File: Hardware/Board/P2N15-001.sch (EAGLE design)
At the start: 30 parts, among them IC1 TLC5941NT, IC2 LTC485N, IC3 74LS07N, IC4 LTC485N

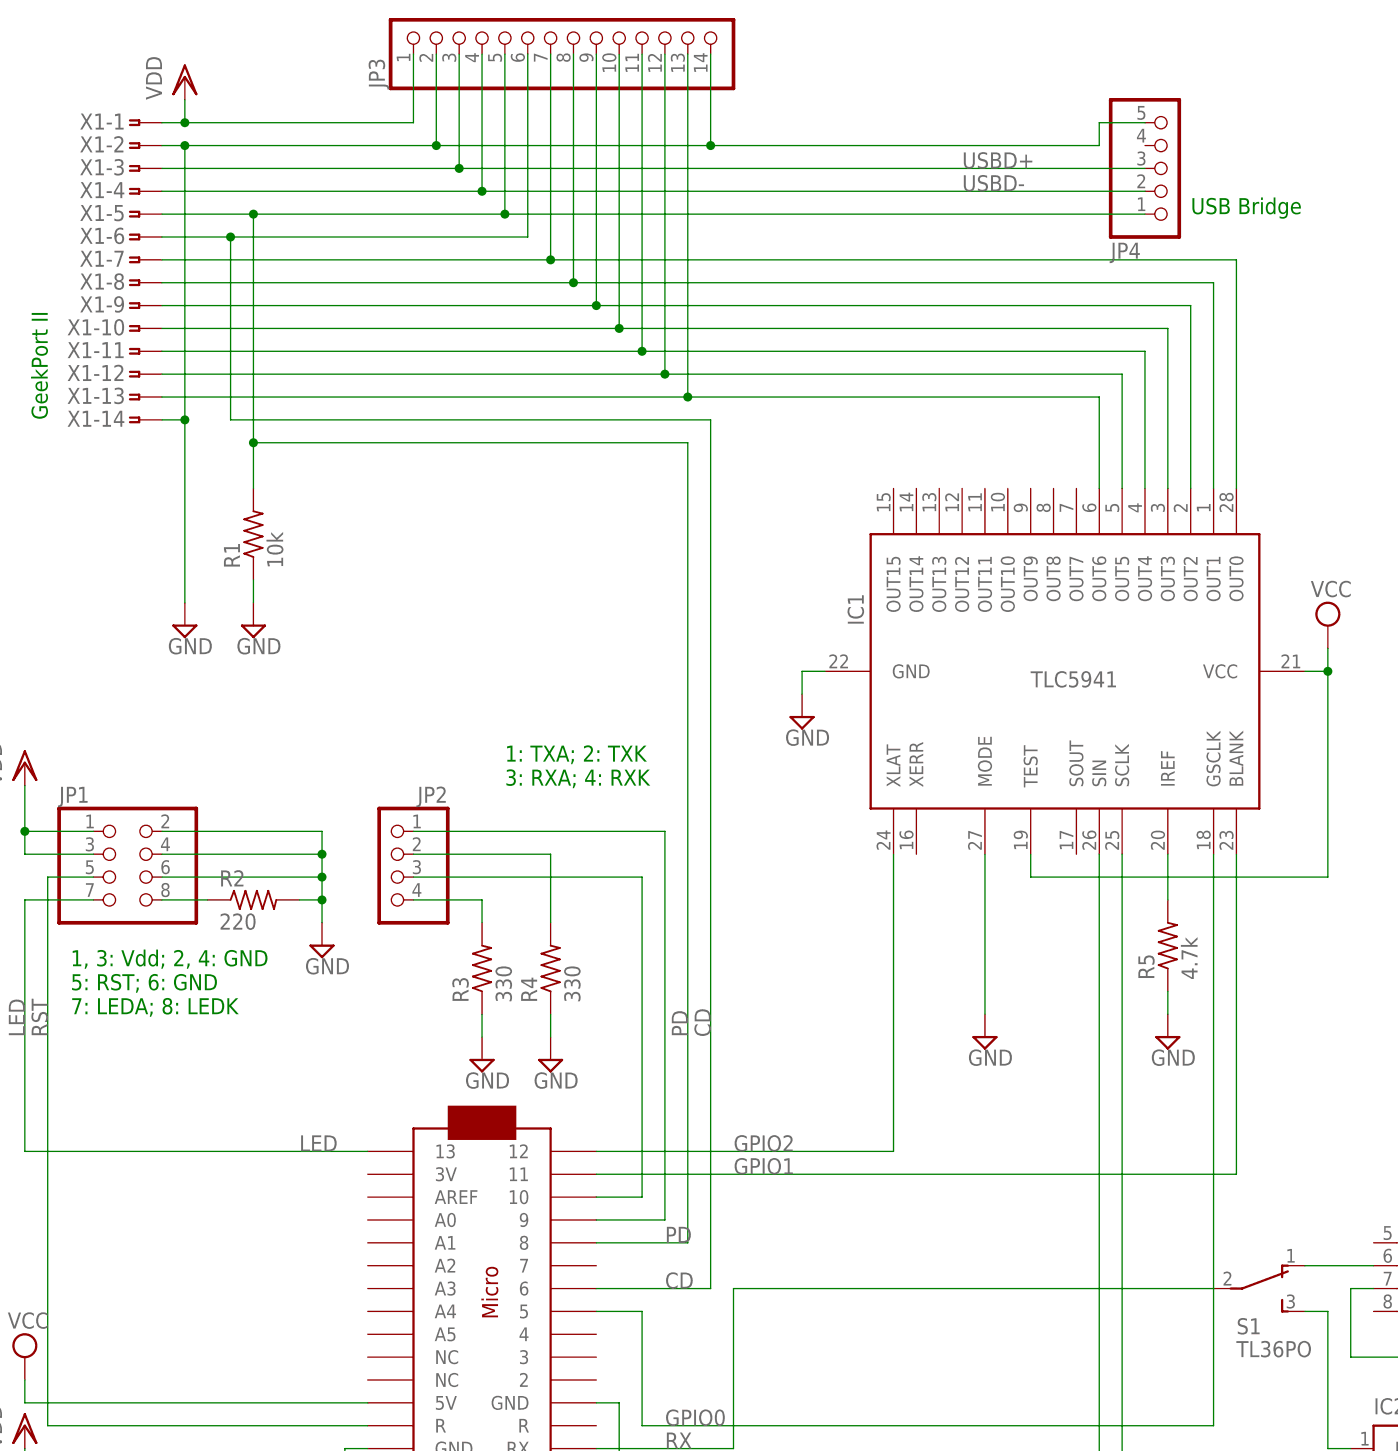
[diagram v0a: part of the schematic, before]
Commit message: Attached LED pattern to GPIO pins.
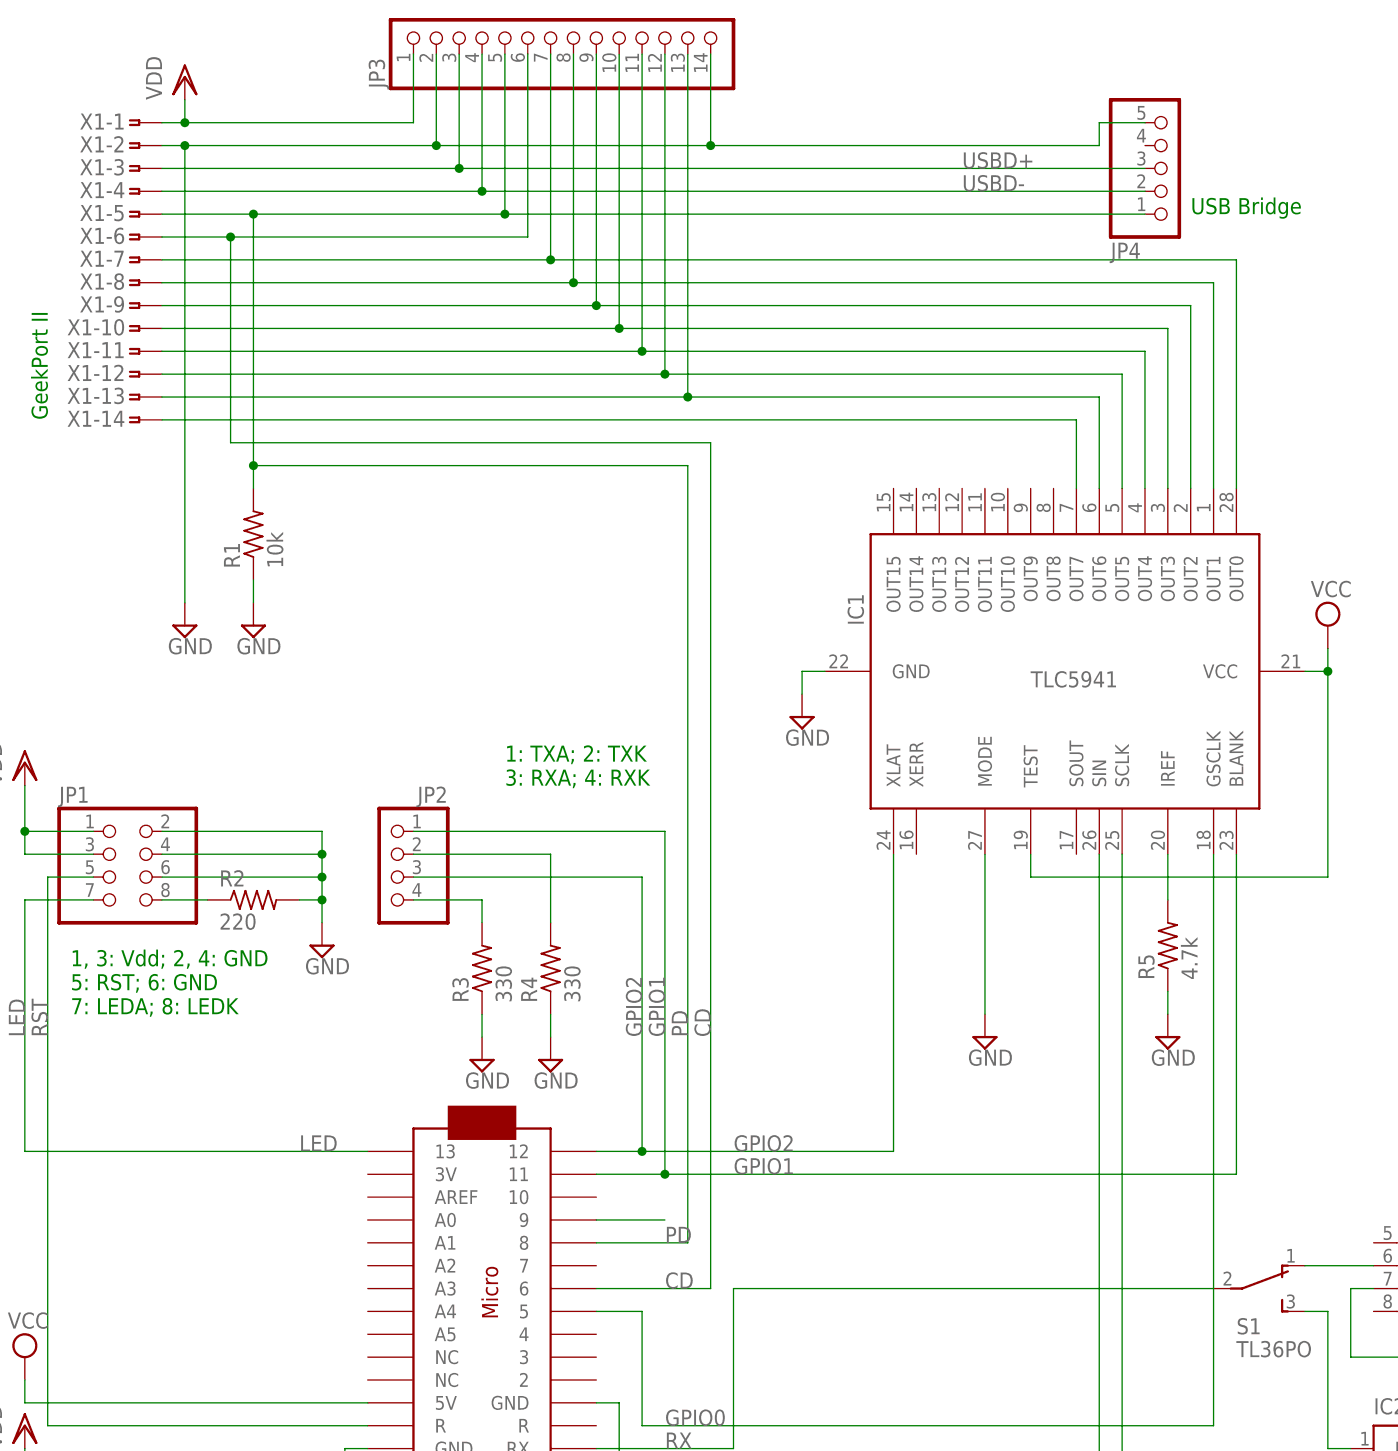
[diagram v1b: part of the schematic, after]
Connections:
- removed net N$5: JP2.3, MC1.10
- new net N$8: IC1.OUT7, X1-14.1
- net GND: no longer X1-14.1
- net GPIO1: now also JP2.1
- net GPIO2: now also JP2.3
- net N$3: no longer JP2.1
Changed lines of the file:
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@@
 <pinref part="SUPPLY2" gate="GND" pin="GND"/>
 <wire x1="22.86" y1="182.88" x2="25.4" y2="182.88" width="0.1524" layer="91"/>
-<wire x1="25.4" y1="182.88" x2="25.4" y2="152.4" width="0.1524" layer="91"/>
-<pinref part="X1" gate="-14" pin="1"/>
-<wire x1="25.4" y1="152.4" x2="25.4" y2="132.08" width="0.1524" layer="91"/>
-<wire x1="22.86" y1="152.4" x2="25.4" y2="152.4" width="0.1524" layer="91"/>
-<junction x="25.4" y="152.4"/>
+<wire x1="25.4" y1="182.88" x2="25.4" y2="132.08" width="0.1524" layer="91"/>
 <wire x1="25.4" y1="182.88" x2="53.34" y2="182.88" width="0.1524" layer="91"/>
 <wire x1="53.34" y1="182.88" x2="83.82" y2="182.88" width="0.1524" layer="91"/>
@@
 <segment>
 <pinref part="MC1" gate="G$1" pin="11"/>
-<wire x1="71.12" y1="68.58" x2="142.24" y2="68.58" width="0.1524" layer="91"/>
+<wire x1="71.12" y1="68.58" x2="78.74" y2="68.58" width="0.1524" layer="91"/>
 <label x="86.36" y="68.58" size="1.778" layer="95"/>
 <pinref part="IC1" gate="G$1" pin="BLANK"/>
+<wire x1="78.74" y1="68.58" x2="142.24" y2="68.58" width="0.1524" layer="91"/>
 <wire x1="142.24" y1="68.58" x2="142.24" y2="104.14" width="0.1524" layer="91"/>
+<pinref part="JP2" gate="A" pin="1"/>
+<wire x1="50.8" y1="106.68" x2="78.74" y2="106.68" width="0.1524" layer="91"/>
+<wire x1="78.74" y1="106.68" x2="78.74" y2="68.58" width="0.1524" layer="91"/>
+<junction x="78.74" y="68.58"/>
+<label x="78.74" y="83.82" size="1.778" layer="95" rot="R90"/>
 </segment>
 </net>
@@
 <wire x1="33.02" y1="175.26" x2="60.96" y2="175.26" width="0.1524" layer="91"/>
 <wire x1="60.96" y1="175.26" x2="132.08" y2="175.26" width="0.1524" layer="91"/>
-<wire x1="33.02" y1="175.26" x2="33.02" y2="149.86" width="0.1524" layer="91"/>
+<wire x1="33.02" y1="175.26" x2="33.02" y2="147.32" width="0.1524" layer="91"/>
 <pinref part="R1" gate="G$1" pin="2"/>
 <junction x="33.02" y="175.26"/>
-<wire x1="33.02" y1="149.86" x2="33.02" y2="144.78" width="0.1524" layer="91"/>
-<wire x1="33.02" y1="149.86" x2="81.28" y2="149.86" width="0.1524" layer="91"/>
-<junction x="33.02" y="149.86"/>
-<wire x1="81.28" y1="149.86" x2="81.28" y2="60.96" width="0.1524" layer="91"/>
+<wire x1="33.02" y1="147.32" x2="33.02" y2="144.78" width="0.1524" layer="91"/>
+<wire x1="33.02" y1="147.32" x2="81.28" y2="147.32" width="0.1524" layer="91"/>
+<junction x="33.02" y="147.32"/>
+<wire x1="81.28" y1="147.32" x2="81.28" y2="60.96" width="0.1524" layer="91"/>
 <pinref part="MC1" gate="G$1" pin="8"/>
 <wire x1="81.28" y1="60.96" x2="71.12" y2="60.96" width="0.1524" layer="91"/>
@@
 <pinref part="X1" gate="-6" pin="1"/>
 <wire x1="22.86" y1="172.72" x2="30.48" y2="172.72" width="0.1524" layer="91"/>
-<wire x1="30.48" y1="172.72" x2="30.48" y2="152.4" width="0.1524" layer="91"/>
-<wire x1="30.48" y1="152.4" x2="83.82" y2="152.4" width="0.1524" layer="91"/>
-<wire x1="83.82" y1="152.4" x2="83.82" y2="55.88" width="0.1524" layer="91"/>
+<wire x1="30.48" y1="172.72" x2="30.48" y2="149.86" width="0.1524" layer="91"/>
+<wire x1="30.48" y1="149.86" x2="83.82" y2="149.86" width="0.1524" layer="91"/>
+<wire x1="83.82" y1="149.86" x2="83.82" y2="55.88" width="0.1524" layer="91"/>
 <pinref part="MC1" gate="G$1" pin="6"/>
 <wire x1="83.82" y1="55.88" x2="71.12" y2="55.88" width="0.1524" layer="91"/>
@@
 <segment>
 <pinref part="MC1" gate="G$1" pin="12"/>
-<wire x1="71.12" y1="71.12" x2="104.14" y2="71.12" width="0.1524" layer="91"/>
+<wire x1="71.12" y1="71.12" x2="76.2" y2="71.12" width="0.1524" layer="91"/>
 <label x="86.36" y="71.12" size="1.778" layer="95"/>
 <pinref part="IC1" gate="G$1" pin="XLAT"/>
+<wire x1="76.2" y1="71.12" x2="104.14" y2="71.12" width="0.1524" layer="91"/>
 <wire x1="104.14" y1="71.12" x2="104.14" y2="104.14" width="0.1524" layer="91"/>
+<pinref part="JP2" gate="A" pin="3"/>
+<wire x1="50.8" y1="101.6" x2="76.2" y2="101.6" width="0.1524" layer="91"/>
+<wire x1="76.2" y1="101.6" x2="76.2" y2="71.12" width="0.1524" layer="91"/>
+<junction x="76.2" y="71.12"/>
+<label x="76.2" y="83.82" size="1.778" layer="95" rot="R90"/>
 </segment>
 </net>
@@
 <pinref part="MC1" gate="G$1" pin="9"/>
 <wire x1="71.12" y1="63.5" x2="78.74" y2="63.5" width="0.1524" layer="91"/>
-<pinref part="JP2" gate="A" pin="1"/>
-<wire x1="50.8" y1="106.68" x2="78.74" y2="106.68" width="0.1524" layer="91"/>
-<wire x1="78.74" y1="106.68" x2="78.74" y2="63.5" width="0.1524" layer="91"/>
-</segment>
-</net>
-<net name="N$5" class="0">
-<segment>
-<pinref part="JP2" gate="A" pin="3"/>
-<wire x1="50.8" y1="101.6" x2="76.2" y2="101.6" width="0.1524" layer="91"/>
-<wire x1="76.2" y1="101.6" x2="76.2" y2="66.04" width="0.1524" layer="91"/>
-<pinref part="MC1" gate="G$1" pin="10"/>
-<wire x1="76.2" y1="66.04" x2="71.12" y2="66.04" width="0.1524" layer="91"/>
 </segment>
 </net>
@@
 </segment>
 </net>
+<net name="N$8" class="0">
+<segment>
+<pinref part="X1" gate="-14" pin="1"/>
+<pinref part="IC1" gate="G$1" pin="OUT7"/>
+<wire x1="22.86" y1="152.4" x2="124.46" y2="152.4" width="0.1524" layer="91"/>
+<wire x1="124.46" y1="152.4" x2="124.46" y2="144.78" width="0.1524" layer="91"/>
+</segment>
+</net>

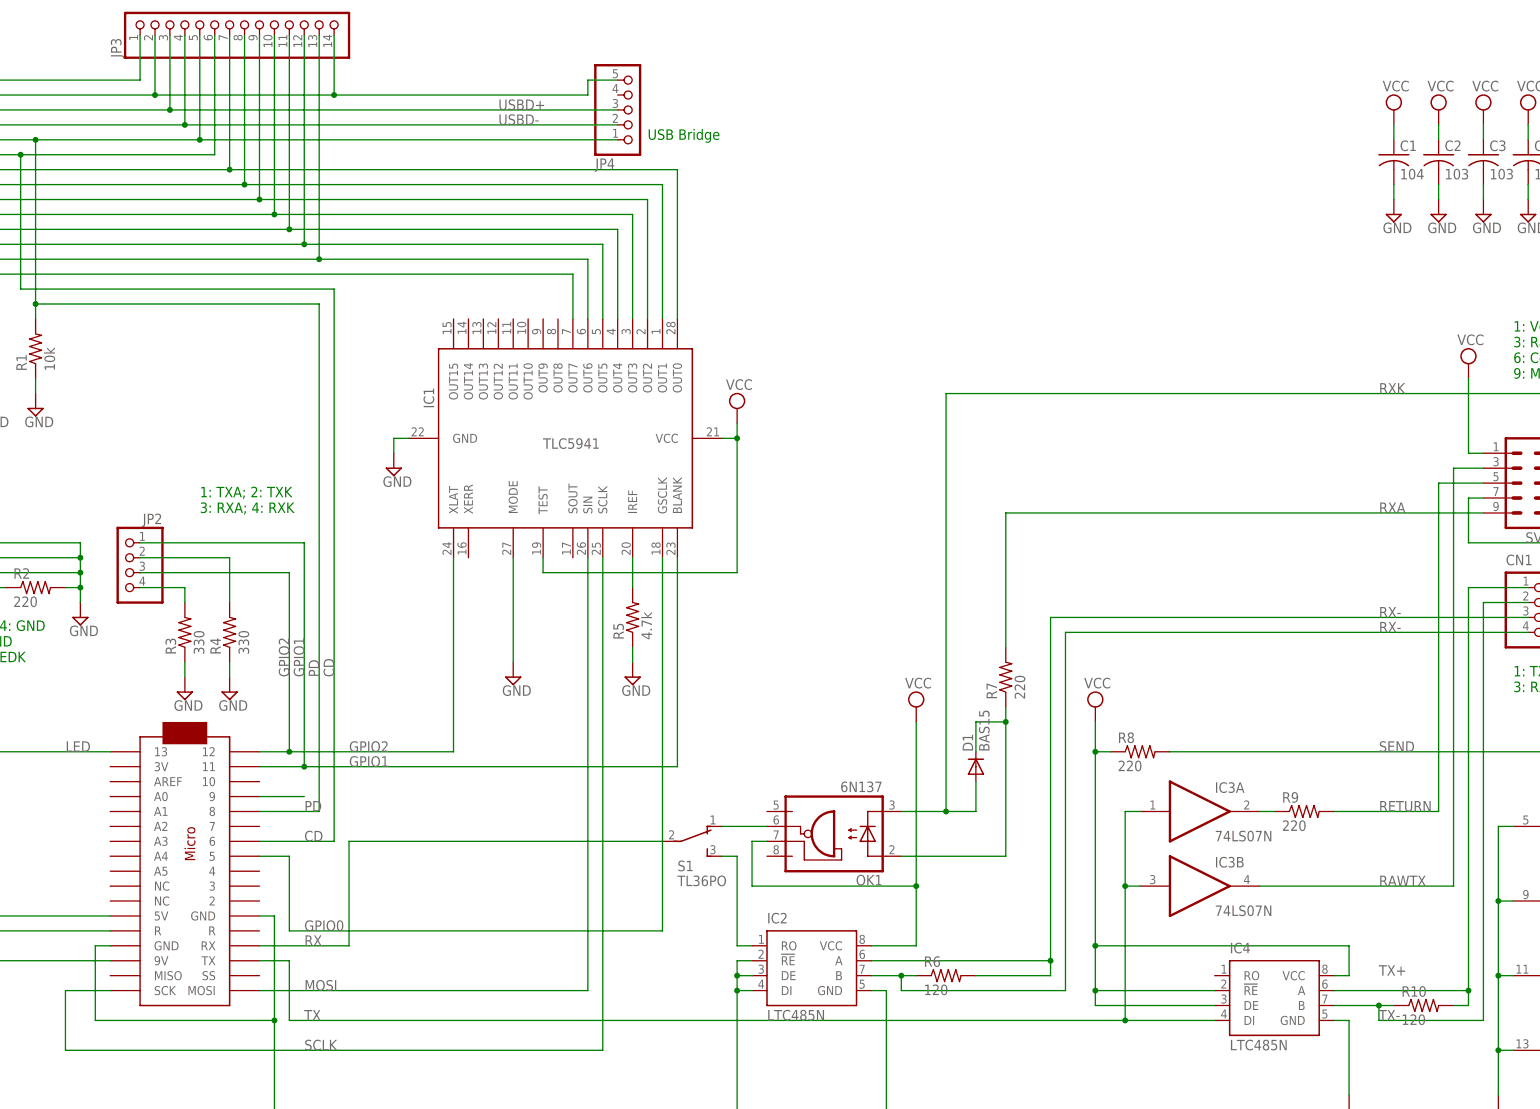
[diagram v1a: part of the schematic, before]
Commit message: Added LED monitors to P2N15.
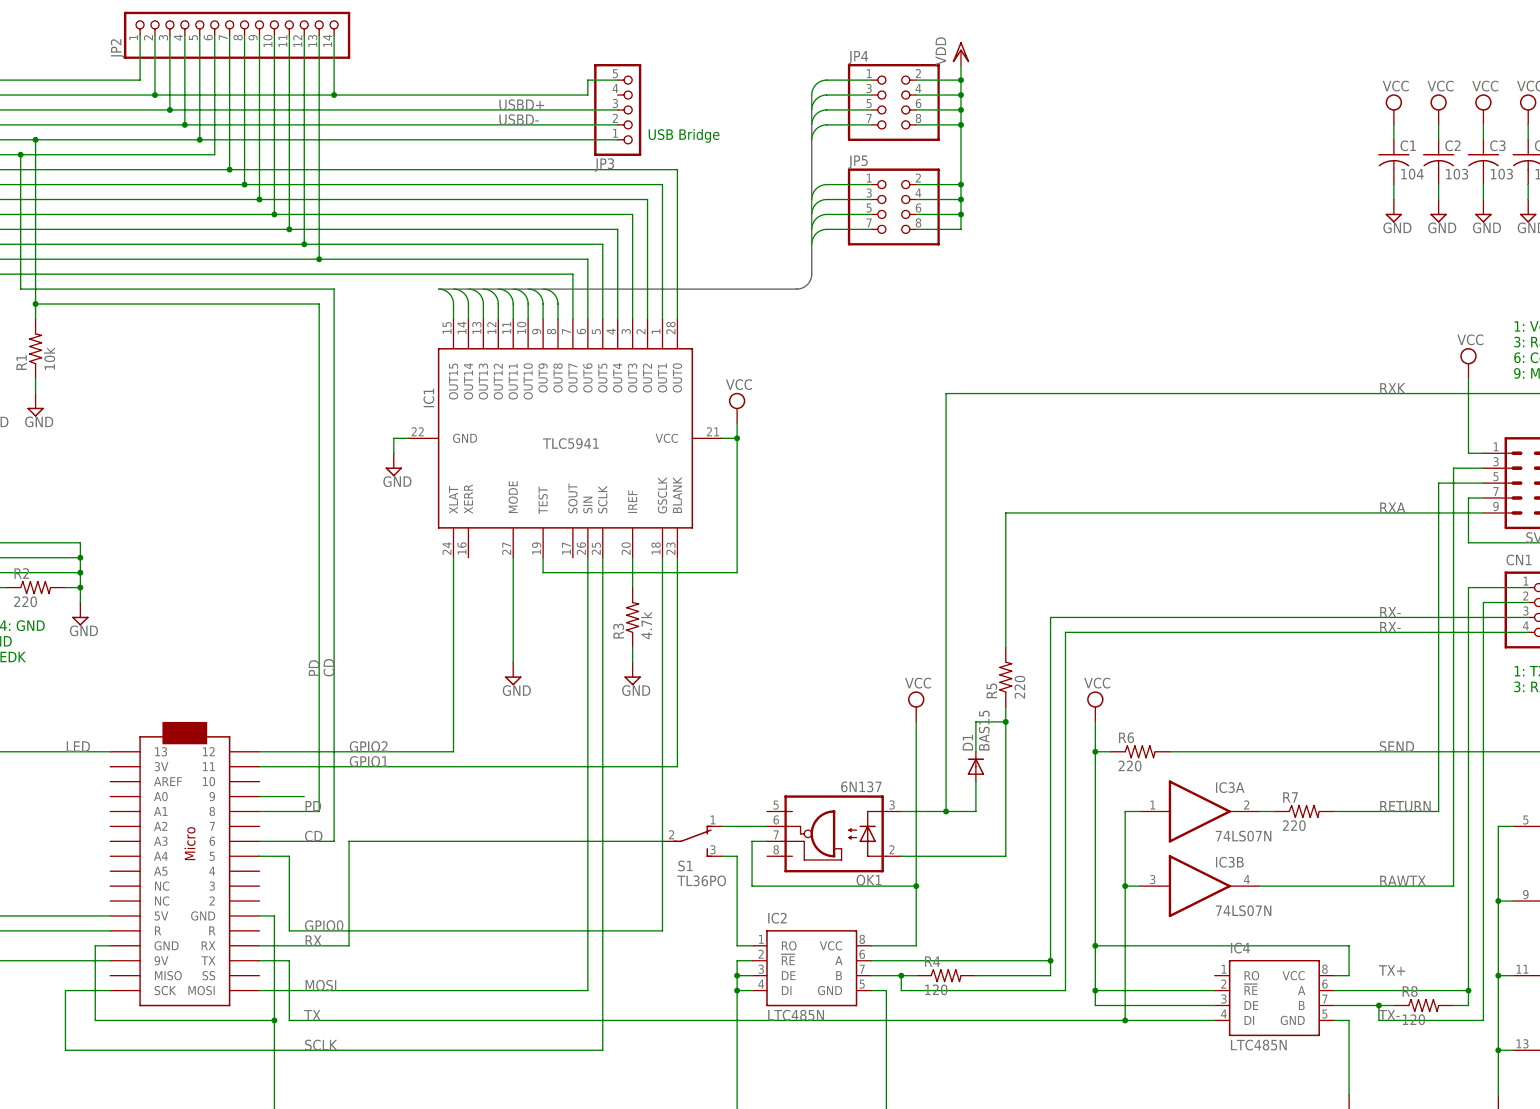
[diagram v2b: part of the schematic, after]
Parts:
- removed R10: 120, resistor:R-US_0204/5
- removed R9: 220, resistor:R-US_0204/5
- added JP5: (no value), pinhead:PINHD-2X4
- JP2: device pinhead:PINHD-1X4 -> pinhead:PINHD-1X14
- JP3: device pinhead:PINHD-1X14 -> pinhead:PINHD-1X5/90
- JP4: device pinhead:PINHD-1X5/90 -> pinhead:PINHD-2X4
- R3: value 330 -> 4.7k
- R4: value 330 -> 120
- R5: value 4.7k -> 220
- R6: value 120 -> 220
- R8: value 220 -> 120
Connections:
- removed net N$6: JP2.2, R4.2
- removed net N$7: JP2.4, R3.2
- new net LED0: IC1.OUT8, JP4.1
- new net LED1: IC1.OUT9, JP4.3
- new net LED2: IC1.OUT10, JP4.5
- new net LED3: IC1.OUT11, JP4.7
- new net LED4: IC1.OUT12, JP5.1
- new net LED5: IC1.OUT13, JP5.3
- new net LED6: IC1.OUT14, JP5.5
- new net LED7: IC1.OUT15, JP5.7
- net ANLG0: now also JP2.8; no longer JP3.8
- net ANLG1: now also JP2.9; no longer JP3.9
- net ANLG2: now also JP2.10; no longer JP3.10
- net ANLG3: now also JP2.11; no longer JP3.11
- net CD: now also JP2.6; no longer JP3.6
- net GND: now also JP2.14, JP2.2, JP3.5; no longer JP3.14, JP3.2, JP4.5, R4.1, R5.1
- net GPIO1: no longer JP2.1
- net GPIO2: no longer JP2.3
- net N$1: now also JP2.7; no longer JP3.7
- net N$15: now also R5.1; no longer R7.1
- net N$2: now also R7.1; no longer R9.1
- net N$28: now also JP2.12; no longer JP3.12
- net N$29: now also JP2.13; no longer JP3.13
- net N$4: now also R3.2; no longer R5.2
- net PD: now also JP2.5, JP3.1; no longer JP3.5, JP4.1
- net RETURN: now also R7.2; no longer R9.2
- net RX+: now also R4.2; no longer R6.2
- net RX-: now also R4.1; no longer R6.1
- net RXA: now also R5.2; no longer R7.2
- net SEND: now also R6.2; no longer R8.2
- net TX+: now also R8.2; no longer R10.2
- net TX-: now also R8.1; no longer R10.1
- net USBD+: now also JP2.3; no longer JP4.3
- net USBD-: now also JP2.4, JP3.2; no longer JP3.4, JP4.2
- net VCC: now also R6.1; no longer R8.1
- net VDD: now also JP2.1, JP4.2, JP4.4, JP4.6, JP4.8, JP5.2, JP5.4, JP5.6, JP5.8; no longer JP3.1
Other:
- note removed: "1: TXA; 2: TXK 3: RXA; 4: RXK"
- moved on the sheet: R3, R4, R5, R6, R7, R8
